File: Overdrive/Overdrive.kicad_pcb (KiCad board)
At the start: 2 copper layers, 70 x 100 mm, 49 parts, among them J1 DC IN, J2 9V battery, J4 IN, J5 OUT, Q1 MMBT2222A, Q2 MMBT2222A, U1 TL072, U2 TL072

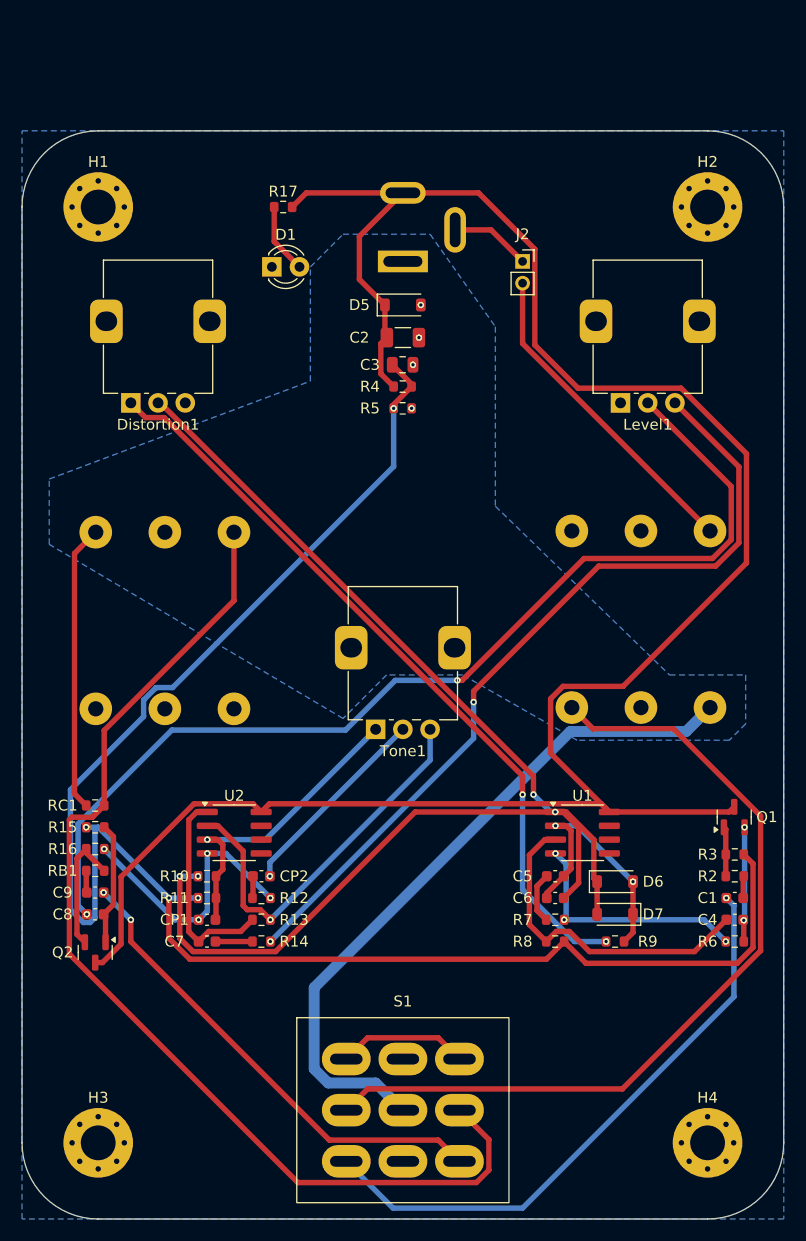
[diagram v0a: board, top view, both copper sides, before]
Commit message: last commit before changing PCB layout to match Delay Pedal shape (110mmx60mm).
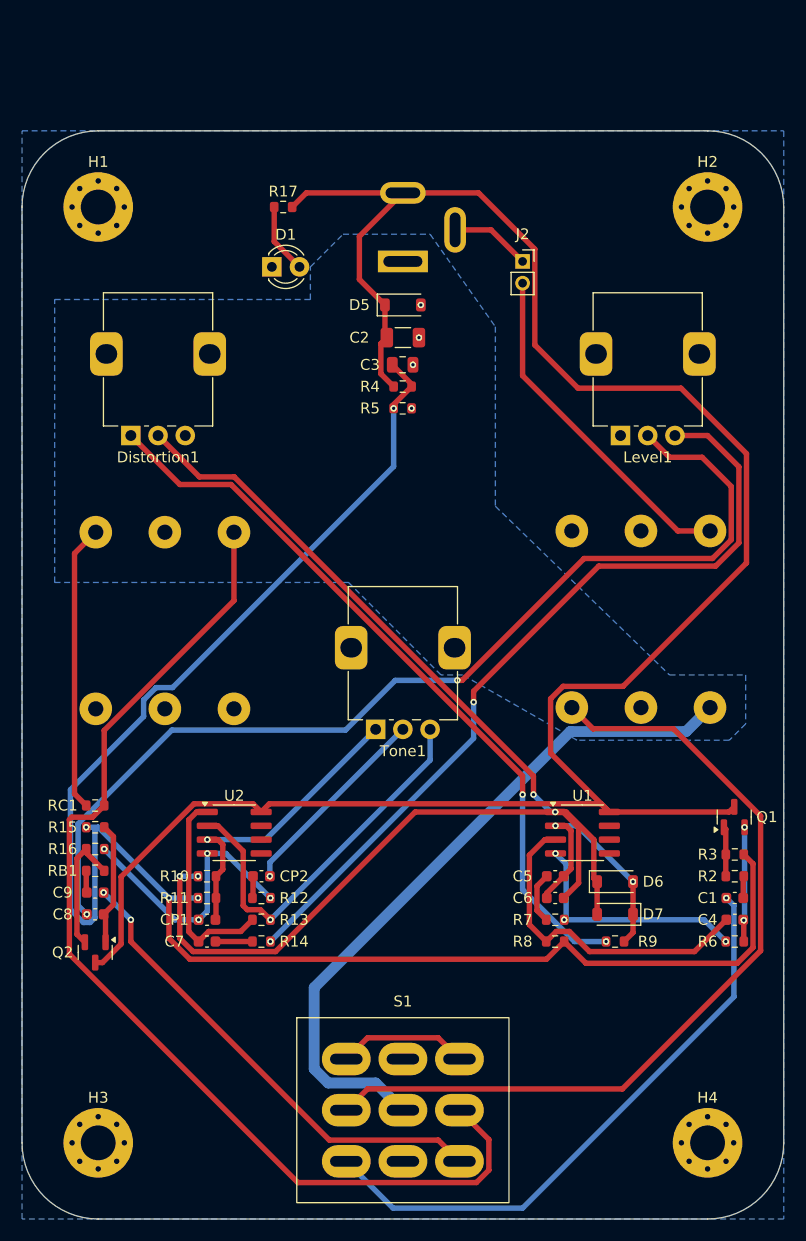
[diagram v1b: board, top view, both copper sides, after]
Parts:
- moved Distortion1 3.00 mm to (125.0, 78.0)
- moved Level1 3.00 mm to (170.0, 78.0)
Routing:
- net /-ve: track 29.9 -> 31.6 mm
- net Net-(Distortion1-Pad1): track 70.3 -> 69.1 mm
- net Net-(C8-Pad1): track 95.2 -> 94.0 mm
- net Net-(Level1-Pad3): track 76.1 -> 74.8 mm
- net Net-(D6-K): track 121.2 -> 120.2 mm
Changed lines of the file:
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@@
 	(footprint "Potentiometer_THT:Potentiometer_RK097_Single_Vertical"
 		(layer "F.Cu")
-		(at 125 75 90)
+		(at 125 78 90)
 		(descr "113004U 1130A6S 11300DR 1130A8G 1130081 1130A5R 1130AP5 1130AST  D1130C3W D1130C1B D1130C3C D1130C2P Potentiometer, vertical, Alps RK09K Single, https://tech.alpsalpine.com/prod/e/pdf/potentiometer/rotarypotentiometers/rk09k/rk09k.pdf")
 		(tags "Potentiometer vertical Alps RK09K RK09D Single Snapin")
@@
 	(footprint "Potentiometer_THT:Potentiometer_RK097_Single_Vertical"
 		(layer "F.Cu")
-		(at 170 75 90)
+		(at 170 78 90)
 		(descr "113004U 1130A6S 11300DR 1130A8G 1130081 1130A5R 1130AP5 1130AST  D1130C3W D1130C1B D1130C3C D1130C2P Potentiometer, vertical, Alps RK09K Single, https://tech.alpsalpine.com/prod/e/pdf/potentiometer/rotarypotentiometers/rk09k/rk09k.pdf")
 		(tags "Potentiometer vertical Alps RK09K RK09D Single Snapin")
@@
 	)
 	(segment
+		(start 166.649472 89.299)
+		(end 155.448472 100.5)
+		(width 0.5)
+		(layer "F.Cu")
+		(net 15)
+	)
+	(segment
 		(start 180.176 82.676)
 		(end 180.176 87.578131)
@@
 	)
 	(segment
-		(start 166.649472 89.299)
-		(end 155.448472 100.5)
+		(start 172.5 78)
+		(end 174.5 80)
 		(width 0.5)
 		(layer "F.Cu")
@@
 	)
 	(segment
-		(start 180.176 87.578131)
-		(end 178.455131 89.299)
+		(start 178.455131 89.299)
+		(end 166.649472 89.299)
+		(width 0.5)
+		(layer "F.Cu")
+		(net 15)
+	)
+	(segment
+		(start 174.5 80)
+		(end 177.5 80)
 		(width 0.5)
 		(layer "F.Cu")
@@
 	)
 	(segment
-		(start 172.5 75)
-		(end 180.176 82.676)
+		(start 180.176 87.578131)
+		(end 178.455131 89.299)
 		(width 0.5)
 		(layer "F.Cu")
@@
 	)
 	(segment
-		(start 178.455131 89.299)
-		(end 166.649472 89.299)
+		(start 177.5 80)
+		(end 180.176 82.676)
 		(width 0.5)
 		(layer "F.Cu")
@@
 	)
 	(segment
-		(start 126.351 76.351)
-		(end 125 75)
+		(start 129.5 82.5)
+		(end 125 78)
 		(width 0.5)
 		(layer "F.Cu")
@@
 	)
 	(segment
-		(start 161 109.291397)
-		(end 128.059603 76.351)
+		(start 161 111)
+		(end 161 109.291397)
 		(width 0.5)
 		(layer "F.Cu")
@@
 	)
 	(segment
-		(start 128.059603 76.351)
-		(end 126.351 76.351)
+		(start 161 109.291397)
+		(end 134.208603 82.5)
 		(width 0.5)
 		(layer "F.Cu")
@@
 	)
 	(segment
-		(start 161 111)
-		(end 161 109.291397)
+		(start 134.208603 82.5)
+		(end 129.5 82.5)
 		(width 0.5)
 		(layer "F.Cu")
@@
 	)
 	(segment
+		(start 131.299 81.799)
+		(end 127.5 78)
+		(width 0.5)
+		(layer "F.Cu")
+		(net 21)
+	)
+	(segment
 		(start 164.999999 112.595)
 		(end 167.549 115.144001)
@@
 	)
 	(segment
+		(start 162 109.300033)
+		(end 134.498967 81.799)
+		(width 0.5)
+		(layer "F.Cu")
+		(net 21)
+	)
+	(segment
 		(start 167.85 119)
 		(end 167.85 122)
@@
 	)
 	(segment
-		(start 166.152 119.123)
-		(end 164.775 120.5)
+		(start 134.498967 81.799)
+		(end 131.299 81.799)
 		(width 0.5)
 		(layer "F.Cu")
@@
 	)
 	(segment
-		(start 162 109.300033)
-		(end 162 111)
+		(start 166.152 119.123)
+		(end 164.775 120.5)
 		(width 0.5)
 		(layer "F.Cu")
@@
 	)
 	(segment
-		(start 127.699967 75)
-		(end 162 109.300033)
+		(start 151.131196 112.595)
+		(end 138.300196 125.426)
 		(width 0.5)
 		(layer "F.Cu")
@@
 	)
 	(segment
-		(start 151.131196 112.595)
-		(end 138.300196 125.426)
+		(start 162 109.300033)
+		(end 162 111)
 		(width 0.5)
 		(layer "F.Cu")
@@
 	)
 	(segment
-		(start 161 64)
-		(end 161 69.545)
+		(start 161 72.5)
+		(end 175.27 86.77)
 		(width 0.5)
 		(layer "F.Cu")
@@
 	)
 	(segment
-		(start 161 69.545)
+		(start 175.27 86.77)
 		(end 178.225 86.77)
 		(width 0.5)
@@
 	)
 	(segment
+		(start 161 64)
+		(end 161 72.5)
+		(width 0.5)
+		(layer "F.Cu")
+		(net 28)
+	)
+	(segment
+		(start 156.5 102.5)
+		(end 156.5 101.5)
+		(width 0.5)
+		(layer "F.Cu")
+		(net 30)
+	)
+	(segment
 		(start 178.745495 90)
 		(end 180.877 87.868495)
@@
 	)
 	(segment
-		(start 156.5 101.5)
-		(end 168 90)
+		(start 180.877 87.868495)
+		(end 180.877 80.877)
 		(width 0.5)
 		(layer "F.Cu")
@@
 	)
 	(segment
-		(start 156.5 102.5)
-		(end 156.5 101.5)
+		(start 156.5 101.5)
+		(end 168 90)
 		(width 0.5)
 		(layer "F.Cu")
@@
 	)
 	(segment
-		(start 180.877 80.877)
-		(end 175 75)
+		(start 178 78)
+		(end 175 78)
 		(width 0.5)
 		(layer "F.Cu")
@@
 	)
 	(segment
-		(start 180.877 87.868495)
-		(end 180.877 80.877)
+		(start 180.877 80.877)
+		(end 178 78)
 		(width 0.5)
 		(layer "F.Cu")
@@
 			(pts
 				(xy 144.5 59.5) (xy 152.5 59.5) (xy 158.5 68) (xy 158.5 84.5) (xy 174.5 100) (xy 181.5 100) (xy 181.5 104.5)
-				(xy 180 106) (xy 166 106) (xy 155.5 100) (xy 148.5 100) (xy 144.5 104) (xy 117.5 88) (xy 117.5 82)
-				(xy 141.5 73) (xy 141.5 62.5)
+				(xy 180 106) (xy 166 106) (xy 155.5 100) (xy 153.5 100) (xy 145 91.5) (xy 118 91.5) (xy 118 65.5)
+				(xy 141.5 65.5) (xy 141.5 62.5)
 			)
 		)

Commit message: Redesigned PCB layout to be 110mm x 60mm
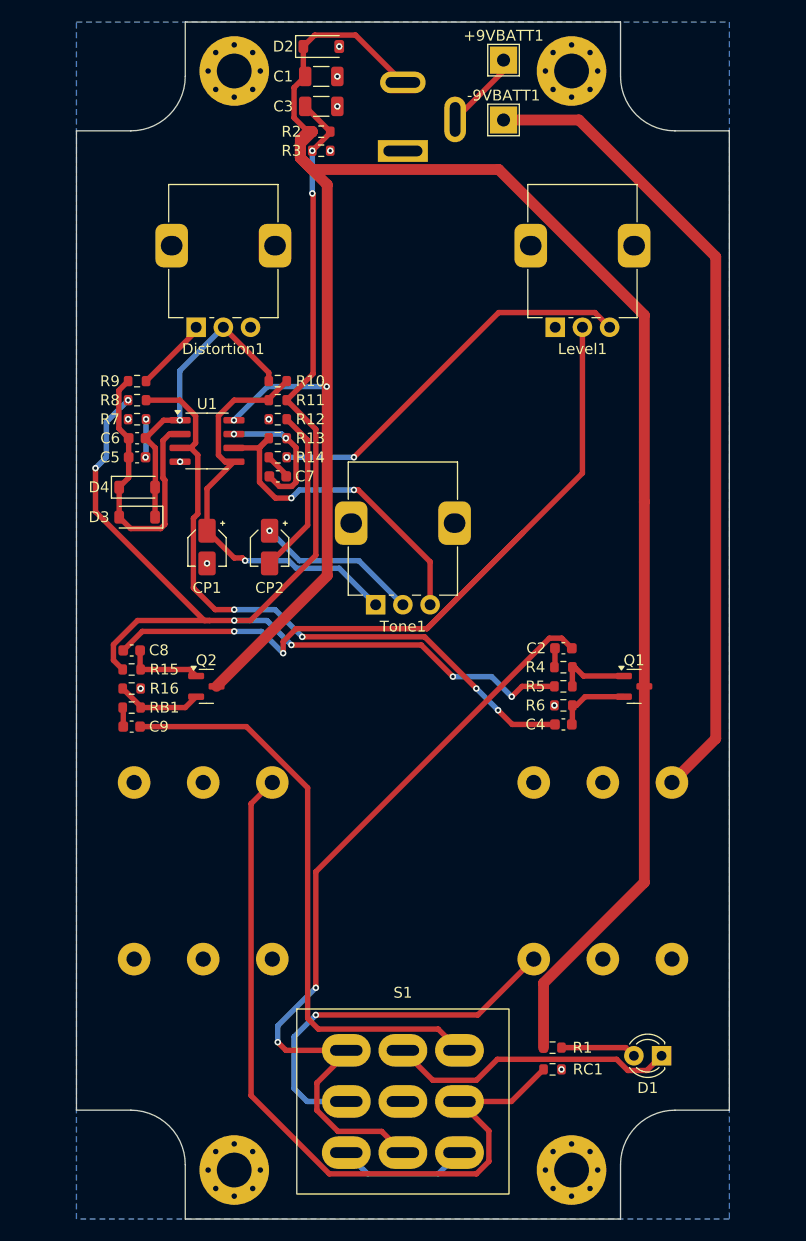
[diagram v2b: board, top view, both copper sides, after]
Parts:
- removed D5, D6, D7: 1N4148W, Diode_SMD:D_SOD-123
- removed J4: IN, Connector_Audio:Jack_6.35mm_Neutrik_NMJ6HFD2_Horizontal
- removed J5: OUT, Connector_Audio:Jack_6.35mm_Neutrik_NMJ6HFD2_Horizontal
- removed R17: 350, Resistor_SMD:R_0603_1608Metric
- removed U2: TL072, Package_SO:SOIC-8_3.9x4.9mm_P1.27mm
- added +9VBATT1: 9V Batt +ve, TestPoint:TestPoint_THTPad_2.5x2.5mm_Drill1.2mm, F.Cu at (159.2, 43.5)
- added -9VBATT1: 9V Batt -ve, TestPoint:TestPoint_THTPad_2.5x2.5mm_Drill1.2mm, F.Cu at (159.2, 49.0)
- added D2: 1N4148W, Diode_SMD:D_SOD-123, F.Cu at (142.5, 42.2)
- added D3: 1N4148W, Diode_SMD:D_SOD-123, F.Cu at (125.6, 85.5)
- added D4: 1N4148W, Diode_SMD:D_SOD-123, F.Cu at (125.6, 82.8)
- added J3: OUT, Connector_Audio:Jack_6.35mm_Neutrik_NMJ6HFD2_Horizontal, B.Cu at (138.0, 109.9)
- added R1: 470R, Resistor_SMD:R_0603_1608Metric, F.Cu at (163.8, 134.2)
- C1: value 20nF -> 100uF; footprint Capacitor_SMD:C_0603_1608Metric -> Capacitor_SMD:C_1206_3216Metric
- C2: value 100uF -> 20nF; footprint Capacitor_SMD:C_1206_3216Metric -> Capacitor_SMD:C_0603_1608Metric
- C3: footprint Capacitor_SMD:C_0805_2012Metric -> Capacitor_SMD:C_1206_3216Metric
- C6: value 51pF -> 47pF
- CP1, CP2: footprint Capacitor_SMD:C_0603_1608Metric -> Capacitor_SMD:CP_Elec_3x5.4
- J1: value DC IN -> IN; footprint Connector_BarrelJack:BarrelJack_GCT_DCJ200-10-A_Horizontal -> Connector_Audio:Jack_6.35mm_Neutrik_NMJ6HFD2_Horizontal
- J2: value 9V battery -> DC IN; footprint Connector_PinSocket_2.00mm:PinSocket_1x02_P2.00mm_Vertical -> Connector_BarrelJack:BarrelJack_GCT_DCJ200-10-A_Horizontal; moved to B.Cu
- R2: value 1k -> 10K
- R3: value 510k -> 10K
- R4: value 10K -> 1k
- R5: value 10K -> 510k
- moved H3 99.3 mm to (134.5, 44.5)
- moved H1 98.6 mm to (165.5, 145.5)
- moved C1 84.5 mm to (142.5, 45.0)
- moved D1 80.9 mm to (173.8, 135.0), turned to 180 degrees
- moved R2 78.3 mm to (142.5, 50.1), turned to 0 degrees
- moved R3 75.0 mm to (142.5, 51.8)
- moved R9 67.7 mm to (125.6, 73.0), turned to 0 degrees
- moved J1 65.2 mm to (162.0, 126.1)
- moved R8 62.9 mm to (125.6, 74.8), turned to 0 degrees
- moved R7 59.9 mm to (125.6, 76.5), turned to 0 degrees
- moved C6 57.1 mm to (125.6, 78.2)
- moved C5 54.4 mm to (125.6, 80.0), turned to 180 degrees
- moved U1 49.9 mm to (132.0, 78.5)
- moved RC1 48.5 mm to (163.8, 136.2), turned to 0 degrees
- moved R11 46.2 mm to (138.5, 74.8), turned to 0 degrees
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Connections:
- net OUT renamed Guitar Out
- C1 pad 1: Net-(C1-Pad1) -> +9V
- C1 pad 2: Net-(C1-Pad2) -> GND
- C2 pad 1: 9V -> Wet In
- C2 pad 2: GND -> Net-(C2-Pad2)
- C3 pad 1: 4.5V -> +4.5V
- C9 pad 2: Net-(C9-Pad2) -> Wet Out
- CP1 pad 2: 0V -> GND
- D1 pad 1: 0V -> Net-(D1-K)
- J2 pad 1: /+ve -> GND
- J2 pad 2: /-ve -> +9V
- Level1 pad 1: 0V -> GND
- Q1 pad 3: 9V -> +9V
- Q2 pad 3: 9V -> +9V
- R11 pad 2: 4.5V -> +4.5V
- R12 pad 1: 0V -> GND
- R15 pad 1: 4.5V -> +4.5V
- R16 pad 2: 0V -> GND
- R2 pad 1: Net-(C1-Pad2) -> +9V
- R2 pad 2: Net-(Q1-B) -> +4.5V
- R3 pad 1: Net-(Q1-B) -> +4.5V
- R3 pad 2: 4.5V -> GND
- R4 pad 1: 9V -> Net-(C2-Pad2)
- R4 pad 2: 4.5V -> Net-(Q1-B)
- R5 pad 1: 4.5V -> Net-(Q1-B)
- R5 pad 2: GND -> +4.5V
- R6 pad 1: 0V -> GND
- R7 pad 1: 0V -> GND
- R8 pad 1: 4.5V -> +4.5V
- S1 pad 1: Net-(S1-Pad1) -> Wet In
- S1 pad 2: IN -> Guitar In
- S1 pad 3: Net-(C1-Pad1) -> Net-(S1-Pad3)
- S1 pad 4: unconnected-(S1-Pad4) -> Net-(D1-K)
- S1 pad 6: 0V -> Wet In
- S1 pad 7: Net-(S1-Pad1) -> Wet Out
- S1 pad 9: Net-(C9-Pad2) -> Net-(S1-Pad3)
- U1 pad 4: 0V -> GND
- U1 pad 5: (no net) -> Net-(CP1-Pad1)
- U1 pad 6: (no net) -> Net-(R13-Pad1)
- U1 pad 7: (no net) -> Net-(C7-Pad1)
- U1 pad 8: 9V -> +9V
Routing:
- net +9V: track 0.00 -> 201.2 mm, vias 0 -> 2
- net 9V: track 193.7 -> 0.00 mm
- net 4.5V: track 158.0 -> 0.00 mm, vias 4 -> 0
- net +4.5V: track 0.00 -> 128.5 mm, vias 0 -> 8
- net Net-(D3-K): track 120.2 -> 28.4 mm, vias 4 -> 1
- net GND: track 90.6 -> 0.07 mm, vias 4 -> 11
- net IN: track 78.0 -> 0.00 mm
- net Net-(-9VBATT1-Pad1): track 0.00 -> 74.7 mm
- net Wet In: track 0.00 -> 72.4 mm, vias 0 -> 2
- net Net-(Distortion1-Pad1): track 69.1 -> 6.86 mm, vias 2 -> 0
- net Net-(C1-Pad1): track 54.8 -> 0.00 mm, vias 1 -> 0
- net Wet Out: track 0.00 -> 54.1 mm
- net 0V: track 47.3 -> 0.00 mm, vias 7 -> 0
- net Net-(C9-Pad2): track 44.1 -> 0.00 mm, vias 2 -> 0
- net Net-(Level1-Pad3): track 74.8 -> 35.7 mm
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- removed copper zone on B.Cu, net 0V
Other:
- board size 70 x 100 mm -> 60 x 110 mm

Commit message: added hard clipping switch, changed electrolytic caps to be THT and to be sources separately.
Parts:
- added SW1: SW_SPDT, Button_Switch_THT:spdt switch custom, F.Cu at (166.5, 81.1)
- CP1, CP2: footprint Capacitor_SMD:CP_Elec_3x5.4 -> Capacitor_THT:CP_Radial_D5.0mm_P2.50mm
- moved CP1 0.50 mm to (131.5, 88.2)
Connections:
- C5 pad 2: Net-(D3-A) -> Net-(SW1-C)
- C6 pad 1: Net-(D3-A) -> Net-(SW1-C)
- R9 pad 1: Net-(D3-A) -> Net-(SW1-C)
- U1 pad 2: Net-(D3-A) -> Net-(SW1-C)
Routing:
- net Net-(SW1-C): track 0.00 -> 77.4 mm, vias 0 -> 4
- net Net-(D3-A): track 28.0 -> 76.0 mm, vias 0 -> 2
- net Net-(CP1-Pad1): track 38.6 -> 48.3 mm
- net Net-(C4-Pad2): track 61.0 -> 66.9 mm, vias 4 -> 2
- net +4.5V: track 128.5 -> 131.4 mm, vias 8 -> 6
- net Net-(C8-Pad1): track 77.6 -> 76.1 mm
- net Net-(CP2-Pad2): track 15.5 -> 16.5 mm
- net Net-(CP2-Pad1): track 15.1 -> 14.4 mm, vias 1 -> 0
- net Wet In: track 72.4 -> 73.0 mm, vias 2 -> 4
- net GND: track 0.07 -> 0.00 mm, vias 11 -> 10
